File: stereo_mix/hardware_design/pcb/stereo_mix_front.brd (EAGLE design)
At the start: 75 x 100 mm, 31 parts, among them U1 THONKICONNOLD, U10 THONKICONNOLD, U11 THONKICONNOLD, U12 THONKICONNOLD, U13 THONKICONNOLD, U14 THONKICONNOLD, U15 THONKICONNOLD, U16 THONKICONNOLD, U17 THONKICONNOLD, U18 THONKICONNOLD, U19 THONKICONNOLD, U2 THONKICONNOLD, U20 THONKICONNOLD, U3 THONKICONNOLD, U4 THONKICONNOLD, U5 THONKICONNOLD, U6 THONKICONNOLD, U7 THONKICONNOLD, U8 THONKICONNOLD, U9 THONKICONNOLD

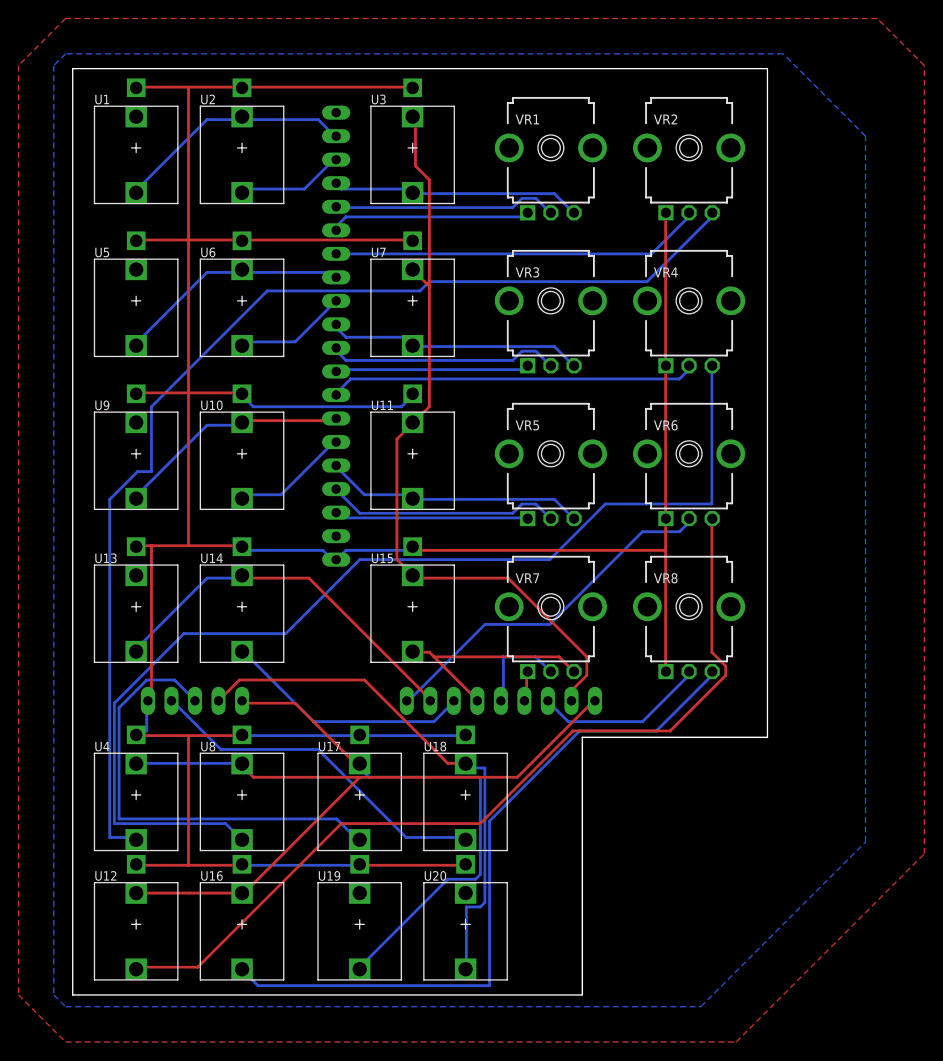
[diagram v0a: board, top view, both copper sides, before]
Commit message: Add new version of stereo_mix_front panel
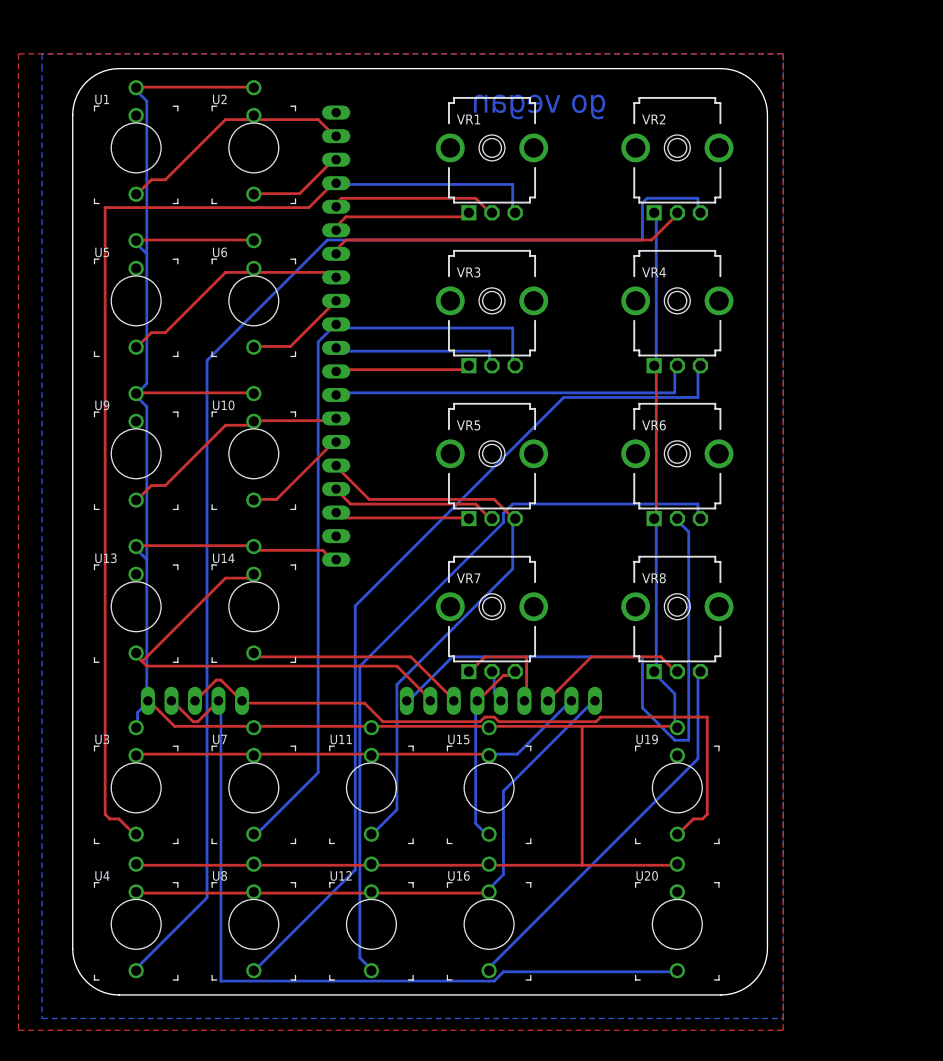
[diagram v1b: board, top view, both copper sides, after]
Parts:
- removed U17, U18: THONKICONNOLD, MusicThingModular:THONKICONN
- U1, U10, U11, U12, U13, U14, U15, U16, U19, U2, U20, U3, U4, U5, U6, U7, U8, U9: value THONKICONNOLD -> WQP-PJ301M-12_JACK; device MusicThingModular:THONKICONN -> jhbruhn-physical:WQP-PJ301M-12_JACK
- VR1, VR2, VR3, VR4, VR5, VR6, VR7, VR8: device MusicThingModular:9MM_SNAP-IN_POT -> jhbruhn-physical:9MM_SNAP-IN_POT
- moved U3 75.3 mm to (6.35, 22.4)
- moved U7 55.3 mm to (19.1, 22.4)
- moved U19 37.3 mm to (64.8, 22.4)
- moved U11 36.3 mm to (31.8, 22.4)
- moved U16 26.7 mm to (44.5, 7.62)
- moved U12 25.4 mm to (31.8, 7.62)
- moved U20 22.9 mm to (64.8, 7.62)
- moved U15 21.2 mm to (44.5, 22.4)
- moved U8 14.0 mm to (19.1, 7.62)
- moved U4 14.0 mm to (6.35, 7.62)
- moved VR1 6.35 mm to (44.8, 91.4)
- moved VR3 6.35 mm to (44.8, 74.9)
- moved VR5 6.35 mm to (44.8, 58.4)
- moved VR7 6.35 mm to (44.8, 41.9)
- moved VR2 1.27 mm to (64.8, 91.4)
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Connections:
- removed net BYPASS_L: JP2.3, U17.P$3_TIP
- removed net BYPASS_R: JP2.4, U18.P$3_TIP
- net 1_IN_L: now also U1.P$1_TIP; no longer U1.P$3_TIP
- net 1_IN_R: now also U2.P$1_TIP; no longer U2.P$3_TIP
- net 1_PAN_CV_IN: now also U3.P$1_TIP; no longer U3.P$3_TIP
- net 2_IN_L: now also U5.P$1_TIP; no longer U5.P$3_TIP
- net 2_IN_R: now also U6.P$1_TIP; no longer U6.P$3_TIP
- net 2_PAN_CV_IN: now also U7.P$1_TIP; no longer U7.P$3_TIP
- net 3_IN_L: now also U9.P$1_TIP; no longer U9.P$3_TIP
- net 3_IN_R: now also U10.P$1_TIP; no longer U10.P$3_TIP
- net 3_PAN_CV_IN: now also U11.P$1_TIP; no longer U11.P$3_TIP
- net 4_IN_L: now also U13.P$1_TIP; no longer U13.P$3_TIP
- net 4_IN_R: now also U14.P$1_TIP; no longer U14.P$3_TIP
- net 4_PAN_CV_IN: now also U15.P$1_TIP; no longer U15.P$3_TIP
- net GND: now also U1.P$3_SLEEVE, U10.P$3_SLEEVE, U11.P$3_SLEEVE, U12.P$3_SLEEVE, U13.P$3_SLEEVE, U14.P$3_SLEEVE, U15.P$3_SLEEVE, U16.P$3_SLEEVE, U19.P$3_SLEEVE, U2.P$3_SLEEVE, U20.P$3_SLEEVE, U3.P$3_SLEEVE, U4.P$3_SLEEVE, U5.P$3_SLEEVE, U6.P$3_SLEEVE, U7.P$3_SLEEVE, U8.P$3_SLEEVE, U9.P$3_SLEEVE; no longer U1.P$1_SLEEVE, U10.P$1_SLEEVE, U11.P$1_SLEEVE, U12.P$1_SLEEVE, U13.P$1_SLEEVE, U14.P$1_SLEEVE, U15.P$1_SLEEVE, U16.P$1_SLEEVE, U17.P$1_SLEEVE, U18.P$1_SLEEVE, U19.P$1_SLEEVE, U2.P$1_SLEEVE, U20.P$1_SLEEVE, U3.P$1_SLEEVE, U4.P$1_SLEEVE, U5.P$1_SLEEVE, U6.P$1_SLEEVE, U7.P$1_SLEEVE, U8.P$1_SLEEVE, U9.P$1_SLEEVE
- net N$13: now also U8.P$1_TIP; no longer U8.P$3_TIP
- net N$17: now also U4.P$1_TIP; no longer U4.P$3_TIP
- net N$21: now also U12.P$1_TIP; no longer U12.P$3_TIP
- net N$28: now also U16.P$1_TIP; no longer U16.P$3_TIP
- net OUT_L: now also JP2.3, U19.P$1_TIP; no longer U17.P$2_SWITCH, U19.P$3_TIP
- net OUT_R: now also JP2.4, U20.P$1_TIP; no longer U18.P$2_SWITCH, U20.P$3_TIP
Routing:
- net 1_PAN_CV_IN: track 27.1 -> 118.1 mm
- net 2_PAN_CV_IN: track 27.8 -> 82.5 mm
- net BYPASS_L: track 49.3 -> 0.00 mm
- net BYPASS_R: track 37.9 -> 0.00 mm
- net N$28: track 76.2 -> 41.7 mm
- net 3_PAN_CV_IN: track 28.2 -> 62.2 mm
- net REF_5: track 82.9 -> 49.8 mm
- net GND: track 355.9 -> 324.9 mm
- net OUT_R: track 57.3 -> 87.0 mm
- net 3_VOLUME_CV: track 38.8 -> 63.7 mm
- net N$13: track 115.8 -> 93.8 mm
- net REF_10: track 83.0 -> 63.7 mm
- net OUT_L: track 57.3 -> 73.3 mm
- net N$21: track 94.4 -> 79.5 mm
- net N$17: track 121.6 -> 133.4 mm
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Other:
- outline, holes or cut-outs redrawn
- board text added: "go vegan"
- board text added: "stereo mix front v1.1 jhbruhn 2020"
